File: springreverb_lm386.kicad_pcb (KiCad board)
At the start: 2 copper layers, 69.9 x 55.3 mm, 54 parts, among them J1 IN, J10 VR2_3, J11 VR_2_2, J12 VR_2GND, J13 To, J14 FromSW, J17 FromGND, J18 From, J19 VR3_1, J2 INGND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

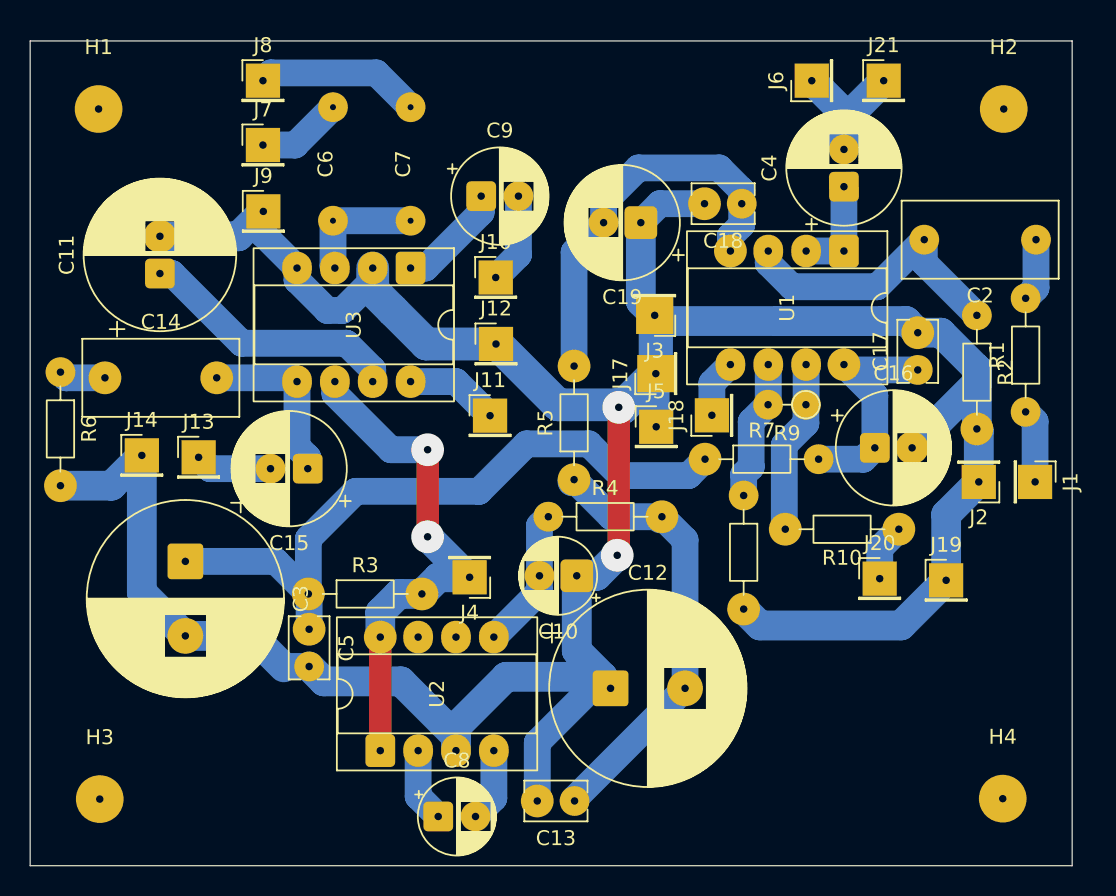
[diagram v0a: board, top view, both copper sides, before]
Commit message: フィルムコンデンサを変更
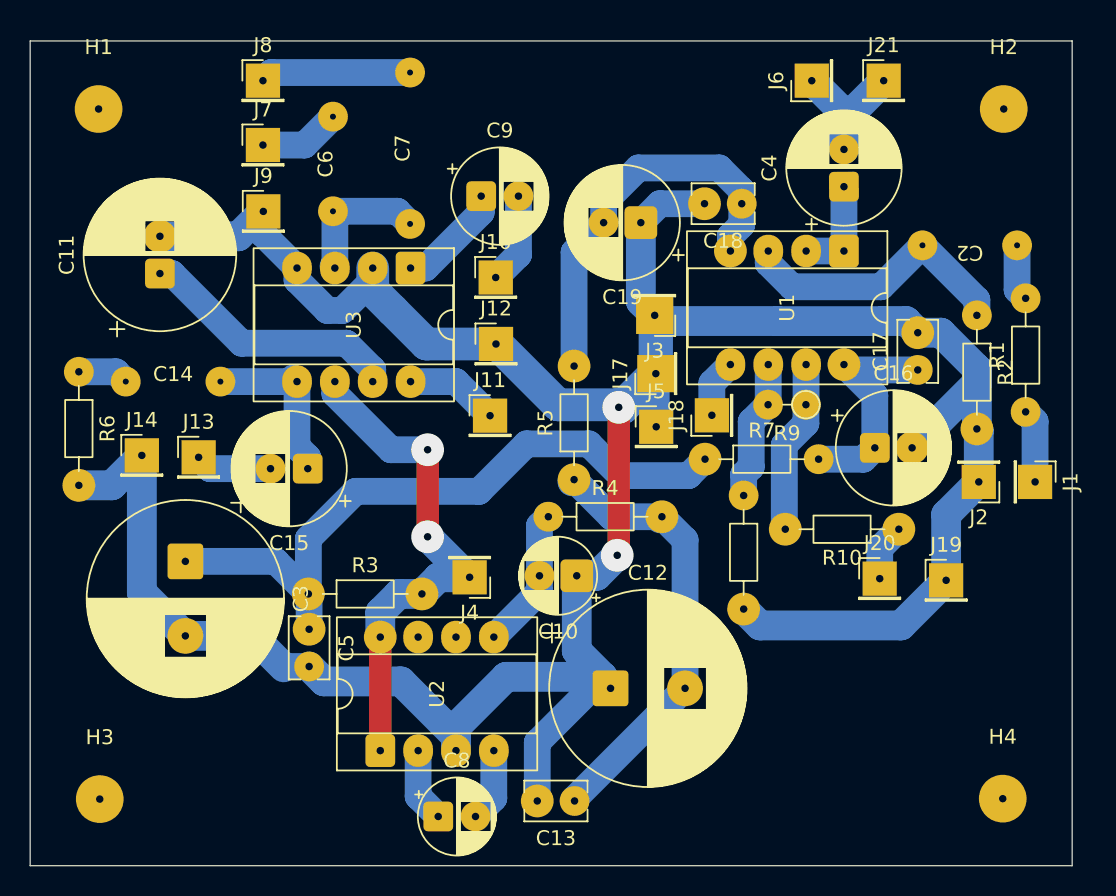
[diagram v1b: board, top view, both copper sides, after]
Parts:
- C14, C2: footprint Capacitor_THT:C_Rect_L10.3mm_W5.0mm_P7.50mm_MKS4 -> MyLibrary:9.3_4.3_p7.5
- C6: footprint MyLibrary:10.5_5.0_p7.5 -> MyLibrary:9.3_4.3_p7.5
- C7: footprint MyLibrary:10.5_5.0_p7.5 -> MyLibrary:11.2_4.3_p10
- H1, H2, H3, H4: footprint MountingHole:MountingHole_3.2mm_M3 -> MyLibrary:MountingHole_3.2mm_M3
- J19: value VR3_1 -> VR3_3
- moved C14 4.58 mm to (58.5, 89.0)
- moved C2 4.46 mm to (111.9, 79.9)
- moved R6 1.23 mm to (52.2, 88.4)
- moved C7 1.06 mm to (74.4, 73.4)
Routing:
- net GND: track 210.5 -> 209.2 mm
- net Net-(U3-+): track 8.43 -> 9.57 mm
- net Net-(J8-Pin_1): track 11.1 -> 10.1 mm
- net Net-(U1A-+): track 19.8 -> 19.2 mm

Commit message: フットプリント修正
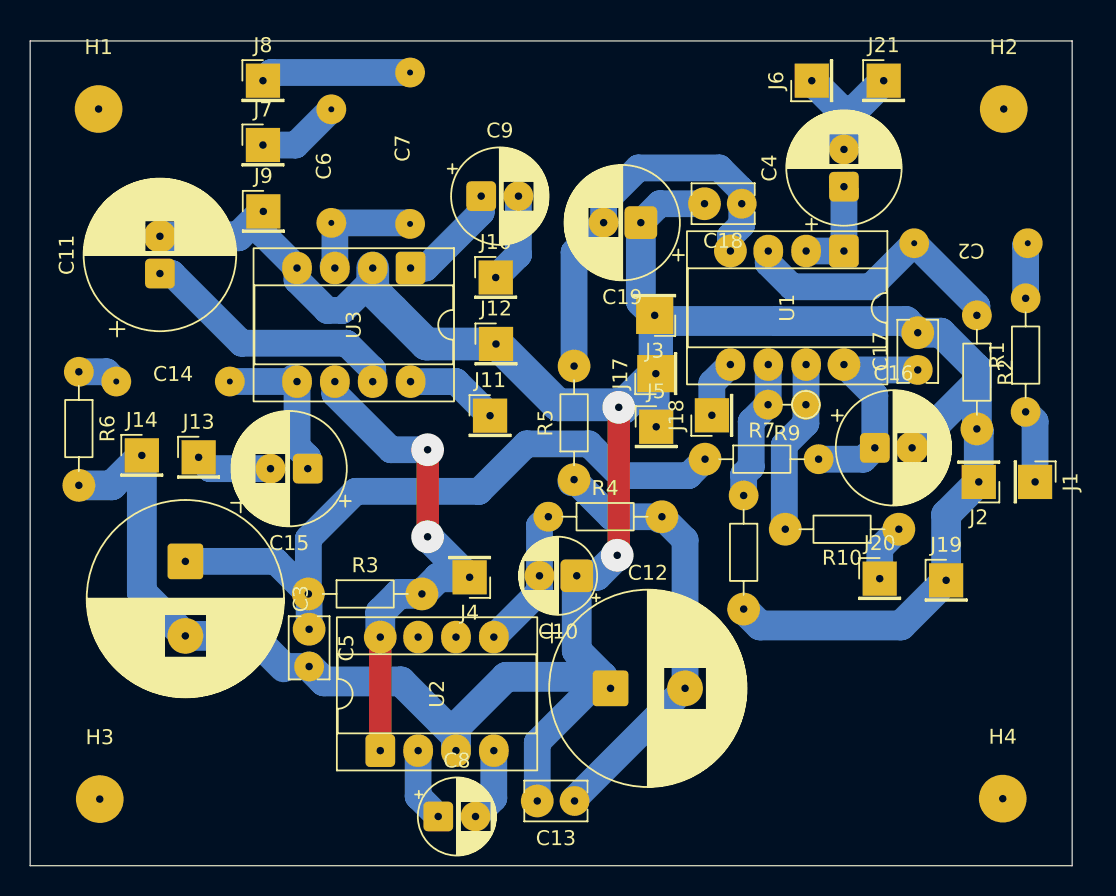
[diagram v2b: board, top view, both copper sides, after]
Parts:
- moved C6 0.18 mm to (69.1, 74.6)
- moved C2 0.16 mm to (112.0, 79.7)
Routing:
- net Net-(U3-+): track 9.57 -> 8.63 mm
- net Net-(C14-Pad1): track 3.42 -> 2.78 mm
- net Net-(C14-Pad2): track 11.6 -> 11.0 mm
